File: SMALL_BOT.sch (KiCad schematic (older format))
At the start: 37 parts, among them J1 MOTOR_B, J10 JMP, J11 UART, J12 LEDS, J13 I2C, J14 LEDS, J15 HEADER_1, J16 HEADER_1, J2 MOTOR_A, J3 HEADER_1, J4 HEADER_1, J5 HC-SR04, J6 HC-SR04, J7 HC-SR04, J8 HC-SR04, J9 Bateria, Q1 2N7002, U1 Teensy4.0_B, U2 DRV8872, U3 LM1117-SOT, U4 DRV8872

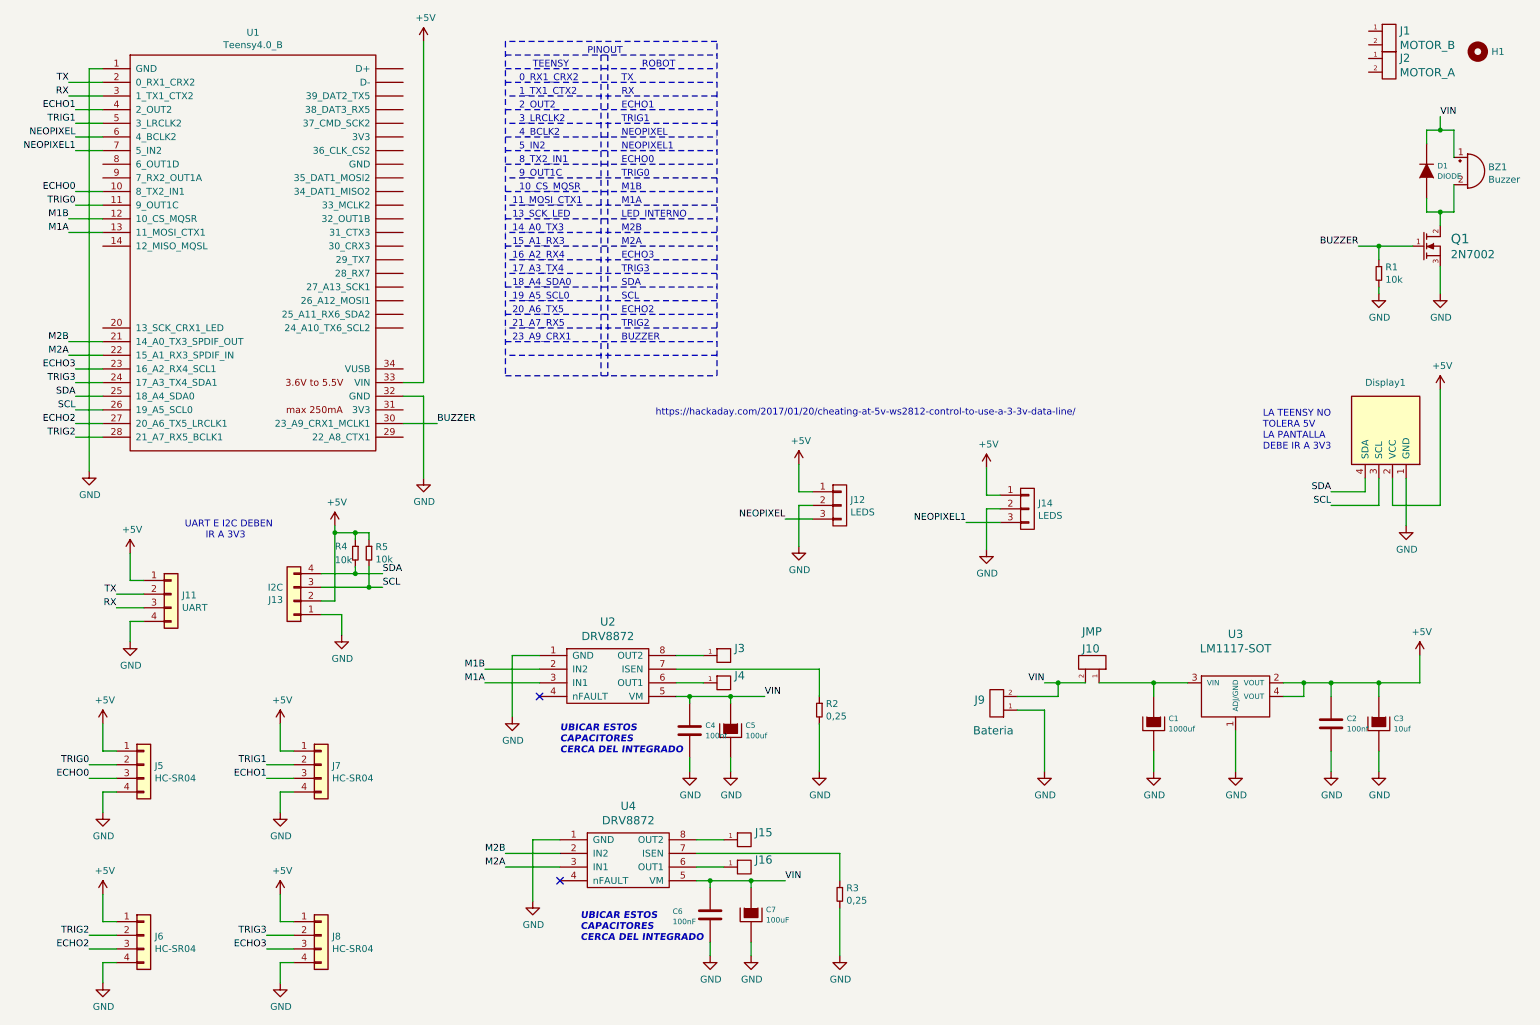
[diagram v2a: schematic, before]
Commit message: modificaciones
se cambio 5v a 3v3, se movieron los capacitores de los drivers de motores
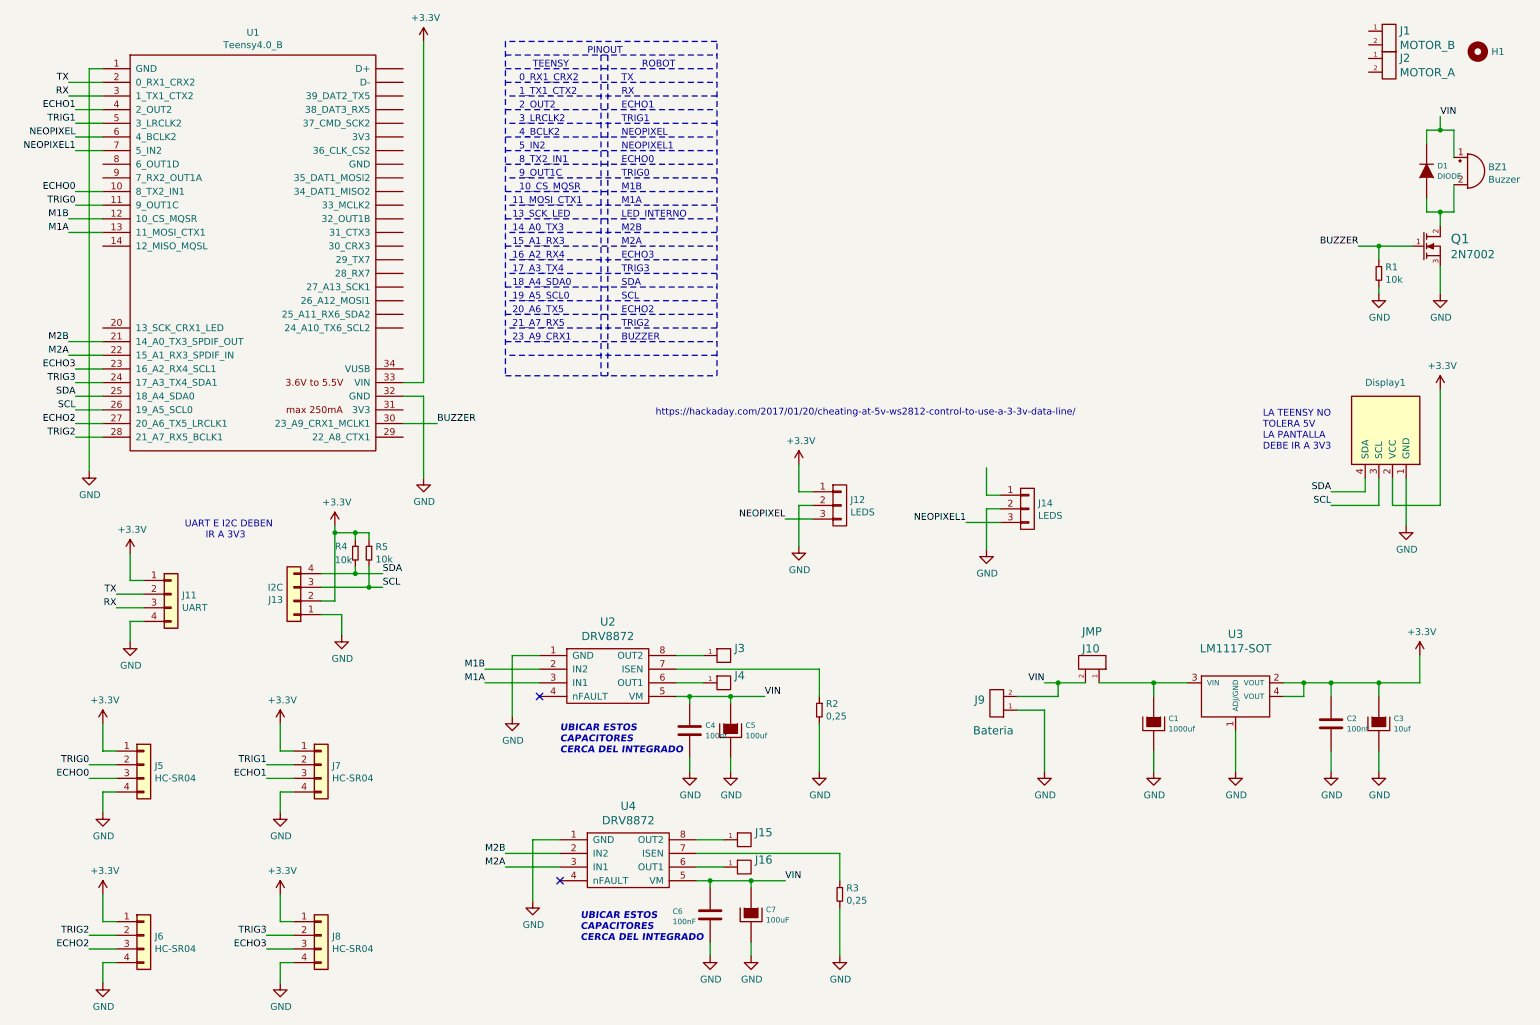
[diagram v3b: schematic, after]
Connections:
- net +5V renamed +3V3
- net +3V3: no longer J14.1 (P1)
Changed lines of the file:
@@
 EESchema Schematic File Version 4
+LIBS:SMALL_BOT-cache
 EELAYER 30 0
 EELAYER END
@@
 Wire Wire Line
 	3250 3250 3250 750
-$Comp
-L power:+5V #PWR0103
-U 1 1 5FC8EC7A
-P 3250 750
-F 0 "#PWR0103" H 3250 600 50  0001 C CNN
-F 1 "+5V" H 3265 923 50  0000 C CNN
-F 2 "" H 3250 750 50  0001 C CNN
-F 3 "" H 3250 750 50  0001 C CNN
-	1    3250 750
-	1    0    0    -1
-$EndComp
 Wire Wire Line
 	3100 3350 3250 3350
@@
 Wire Wire Line
 	900  5950 900  5750
-$Comp
-L power:+5V #PWR0107
-U 1 1 5FCB0796
-P 900 5750
-F 0 "#PWR0107" H 900 5600 50  0001 C CNN
-F 1 "+5V" H 915 5923 50  0000 C CNN
-F 2 "" H 900 5750 50  0001 C CNN
-F 3 "" H 900 5750 50  0001 C CNN
-	1    900  5750
-	1    0    0    -1
-$EndComp
 Wire Wire Line
 	1000 6050 800  6050
@@
 Wire Wire Line
 	2200 5950 2200 5750
-$Comp
-L power:+5V #PWR0109
-U 1 1 5FCB87C3
-P 2200 5750
-F 0 "#PWR0109" H 2200 5600 50  0001 C CNN
-F 1 "+5V" H 2215 5923 50  0000 C CNN
-F 2 "" H 2200 5750 50  0001 C CNN
-F 3 "" H 2200 5750 50  0001 C CNN
-	1    2200 5750
-	1    0    0    -1
-$EndComp
 Wire Wire Line
 	2300 6050 2100 6050
@@
 Wire Wire Line
 	900  7200 900  7000
-$Comp
-L power:+5V #PWR0111
-U 1 1 5FCBB906
-P 900 7000
-F 0 "#PWR0111" H 900 6850 50  0001 C CNN
-F 1 "+5V" H 915 7173 50  0000 C CNN
-F 2 "" H 900 7000 50  0001 C CNN
-F 3 "" H 900 7000 50  0001 C CNN
-	1    900  7000
-	1    0    0    -1
-$EndComp
 Wire Wire Line
 	1000 7300 800  7300
@@
 Wire Wire Line
 	2200 7200 2200 7000
-$Comp
-L power:+5V #PWR0113
-U 1 1 5FCBB92C
-P 2200 7000
-F 0 "#PWR0113" H 2200 6850 50  0001 C CNN
-F 1 "+5V" H 2215 7173 50  0000 C CNN
-F 2 "" H 2200 7000 50  0001 C CNN
-F 3 "" H 2200 7000 50  0001 C CNN
-	1    2200 7000
-	1    0    0    -1
-$EndComp
 Wire Wire Line
 	2300 7300 2100 7300
@@
 	10550 5450 10550 5250
 Connection ~ 10250 5450
-$Comp
-L power:+5V #PWR0120
-U 1 1 5FD35D78
-P 10550 5250
-F 0 "#PWR0120" H 10550 5100 50  0001 C CNN
-F 1 "+5V" H 10565 5423 50  0000 C CNN
-F 2 "" H 10550 5250 50  0001 C CNN
-F 3 "" H 10550 5250 50  0001 C CNN
-	1    10550 5250
-	1    0    0    -1
-$EndComp
 Text Label 7800 5450 2    50   ~ 0
 VIN
@@
 Wire Wire Line
 	1100 4700 1100 4500
-$Comp
-L power:+5V #PWR0121
-U 1 1 5FD6E702
-P 1100 4500
-F 0 "#PWR0121" H 1100 4350 50  0001 C CNN
-F 1 "+5V" H 1115 4673 50  0000 C CNN
-F 2 "" H 1100 4500 50  0001 C CNN
-F 3 "" H 1100 4500 50  0001 C CNN
-	1    1100 4500
-	1    0    0    -1
-$EndComp
 Wire Wire Line
 	1200 5000 1100 5000
@@
 Wire Wire Line
 	6000 4050 6000 3850
-$Comp
-L power:+5V #PWR0124
-U 1 1 5FD9C4FB
-P 6000 3850
-F 0 "#PWR0124" H 6000 3700 50  0001 C CNN
-F 1 "+5V" H 6015 4023 50  0000 C CNN
-F 2 "" H 6000 3850 50  0001 C CNN
-F 3 "" H 6000 3850 50  0001 C CNN
-	1    6000 3850
-	1    0    0    -1
-$EndComp
 Wire Wire Line
 	6100 4150 6000 4150
@@
 	-1   0    0    1
 $EndComp
-$Comp
-L power:+5V #PWR0126
-U 1 1 5FE06332
-P 2600 4300
-F 0 "#PWR0126" H 2600 4150 50  0001 C CNN
-F 1 "+5V" H 2615 4473 50  0000 C CNN
-F 2 "" H 2600 4300 50  0001 C CNN
-F 3 "" H 2600 4300 50  0001 C CNN
-	1    2600 4300
-	1    0    0    -1
-$EndComp
 Text Label 2950 4750 0    50   ~ 0
 SCL
@@
 Wire Wire Line
 	700  3350 900  3350
-$Comp
-L EESTN5:Conn_01X03 J14
-U 1 1 5FE32101
-P 7675 4175
-F 0 "J14" H 7753 4216 50  0000 L CNN
-F 1 "LEDS" H 7753 4125 50  0000 L CNN
-F 2 "EESTN5:Pin_Strip_3" H 7675 4175 50  0001 C CNN
-F 3 "" H 7675 4175 50  0001 C CNN
-	1    7675 4175
-	1    0    0    -1
-$EndComp
-Wire Wire Line
-	7475 4075 7375 4075
-Wire Wire Line
-	7375 4075 7375 3875
-$Comp
-L power:+5V #PWR0128
-U 1 1 5FE32289
-P 7375 3875
-F 0 "#PWR0128" H 7375 3725 50  0001 C CNN
-F 1 "+5V" H 7390 4048 50  0000 C CNN
-F 2 "" H 7375 3875 50  0001 C CNN
-F 3 "" H 7375 3875 50  0001 C CNN
-	1    7375 3875
-	1    0    0    -1
-$EndComp
-Text Label 7225 4275 2    50   ~ 0
-NEOPIXEL1
-$Comp
-L power:GND #PWR0129
-U 1 1 5FE32297
-P 7375 4475
-F 0 "#PWR0129" H 7375 4225 50  0001 C CNN
-F 1 "GND" H 7380 4302 50  0000 C CNN
-F 2 "" H 7375 4475 50  0001 C CNN
-F 3 "" H 7375 4475 50  0001 C CNN
-	1    7375 4475
-	1    0    0    -1
-$EndComp
 Text Label 700  1550 2    50   ~ 0
 NEOPIXEL1
@@
 	1    0    0    -1
 $EndComp
-$Comp
-L power:+5V #PWR0102
-U 1 1 5FE956FC
-P 10700 3300
-F 0 "#PWR0102" H 10700 3150 50  0001 C CNN
-F 1 "+5V" H 10715 3473 50  0000 C CNN
-F 2 "" H 10700 3300 50  0001 C CNN
-F 3 "" H 10700 3300 50  0001 C CNN
-	1    10700 3300
-	1    0    0    -1
-$EndComp
 Text Label 9900 4050 2    50   ~ 0
 SDA
@@
 Wire Wire Line
 	5900 4250 6100 4250
-Wire Wire Line
-	7375 4175 7475 4175
-Wire Wire Line
-	7375 4175 7375 4475
-Wire Wire Line
-	7475 4275 7225 4275
 $Comp
 L EESTN5:R R4
@@
 Text Notes 1500 4400 0    50   ~ 0
 UART E I2C DEBEN \n       IR A 3V3
+$Comp
+L power:+3.3V #PWR0102
+U 1 1 5FEE7BF9
+P 3250 750
+F 0 "#PWR0102" H 3250 600 50  0001 C CNN
+F 1 "+3.3V" H 3265 923 50  0000 C CNN
+F 2 "" H 3250 750 50  0001 C CNN
+F 3 "" H 3250 750 50  0001 C CNN
+	1    3250 750
+	1    0    0    -1
+$EndComp
+$Comp
+L power:+3.3V #PWR0103
+U 1 1 5FEE847A
+P 1100 4500
+F 0 "#PWR0103" H 1100 4350 50  0001 C CNN
+F 1 "+3.3V" H 1115 4673 50  0000 C CNN
+F 2 "" H 1100 4500 50  0001 C CNN
+F 3 "" H 1100 4500 50  0001 C CNN
+	1    1100 4500
+	1    0    0    -1
+$EndComp
+$Comp
+L power:+3.3V #PWR0107
+U 1 1 5FEF8071
+P 2600 4300
+F 0 "#PWR0107" H 2600 4150 50  0001 C CNN
+F 1 "+3.3V" H 2615 4473 50  0000 C CNN
+F 2 "" H 2600 4300 50  0001 C CNN
+F 3 "" H 2600 4300 50  0001 C CNN
+	1    2600 4300
+	1    0    0    -1
+$EndComp
+$Comp
+L power:+3.3V #PWR0109
+U 1 1 5FF075F0
+P 900 5750
+F 0 "#PWR0109" H 900 5600 50  0001 C CNN
+F 1 "+3.3V" H 915 5923 50  0000 C CNN
+F 2 "" H 900 5750 50  0001 C CNN
+F 3 "" H 900 5750 50  0001 C CNN
+	1    900  5750
+	1    0    0    -1
+$EndComp
+$Comp
+L power:+3.3V #PWR0111
+U 1 1 5FF078CA
+P 2200 5750
+F 0 "#PWR0111" H 2200 5600 50  0001 C CNN
+F 1 "+3.3V" H 2215 5923 50  0000 C CNN
+F 2 "" H 2200 5750 50  0001 C CNN
+F 3 "" H 2200 5750 50  0001 C CNN
+	1    2200 5750
+	1    0    0    -1
+$EndComp
+$Comp
+L power:+3.3V #PWR0113
+U 1 1 5FF07D0F
+P 900 7000
+F 0 "#PWR0113" H 900 6850 50  0001 C CNN
+F 1 "+3.3V" H 915 7173 50  0000 C CNN
+F 2 "" H 900 7000 50  0001 C CNN
+F 3 "" H 900 7000 50  0001 C CNN
+	1    900  7000
+	1    0    0    -1
+$EndComp
+$Comp
+L power:+3.3V #PWR0120
+U 1 1 5FF07D19
+P 2200 7000
+F 0 "#PWR0120" H 2200 6850 50  0001 C CNN
+F 1 "+3.3V" H 2215 7173 50  0000 C CNN
+F 2 "" H 2200 7000 50  0001 C CNN
+F 3 "" H 2200 7000 50  0001 C CNN
+	1    2200 7000
+	1    0    0    -1
+$EndComp
+$Comp
+L power:+3.3V #PWR0121
+U 1 1 5FF10294
+P 6000 3850
+F 0 "#PWR0121" H 6000 3700 50  0001 C CNN
+F 1 "+3.3V" H 6015 4023 50  0000 C CNN
+F 2 "" H 6000 3850 50  0001 C CNN
+F 3 "" H 6000 3850 50  0001 C CNN
+	1    6000 3850
+	1    0    0    -1
+$EndComp
+$Comp
+L power:+3.3V #PWR0124
+U 1 1 5FF1029E
+P 10700 3300
+F 0 "#PWR0124" H 10700 3150 50  0001 C CNN
+F 1 "+3.3V" H 10715 3473 50  0000 C CNN
+F 2 "" H 10700 3300 50  0001 C CNN
+F 3 "" H 10700 3300 50  0001 C CNN
+	1    10700 3300
+	1    0    0    -1
+$EndComp
+$Comp
+L EESTN5:Conn_01X03 J14
+U 1 1 5FE32101
+P 7675 4175
+F 0 "J14" H 7753 4216 50  0000 L CNN
+F 1 "LEDS" H 7753 4125 50  0000 L CNN
+F 2 "EESTN5:Pin_Strip_3" H 7675 4175 50  0001 C CNN
+F 3 "" H 7675 4175 50  0001 C CNN
+	1    7675 4175
+	1    0    0    -1
+$EndComp
+Wire Wire Line
+	7475 4075 7375 4075
+Wire Wire Line
+	7375 4075 7375 3875
+$Comp
+L power:GND #PWR0129
+U 1 1 5FE32297
+P 7375 4475
+F 0 "#PWR0129" H 7375 4225 50  0001 C CNN
+F 1 "GND" H 7380 4302 50  0000 C CNN
+F 2 "" H 7375 4475 50  0001 C CNN
+F 3 "" H 7375 4475 50  0001 C CNN
+	1    7375 4475
+	1    0    0    -1
+$EndComp
+Wire Wire Line
+	7375 4175 7475 4175
+Wire Wire Line
+	7375 4175 7375 4475
+Wire Wire Line
+	7475 4275 7225 4275
+Text Label 7225 4275 2    50   ~ 0
+NEOPIXEL1
+$Comp
+L power:+3.3V #PWR0126
+U 1 1 5FF7A377
+P 10550 5250
+F 0 "#PWR0126" H 10550 5100 50  0001 C CNN
+F 1 "+3.3V" H 10565 5423 50  0000 C CNN
+F 2 "" H 10550 5250 50  0001 C CNN
+F 3 "" H 10550 5250 50  0001 C CNN
+	1    10550 5250
+	1    0    0    -1
+$EndComp
 $EndSCHEMATC
